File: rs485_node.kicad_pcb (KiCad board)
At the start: 2 copper layers, 53 x 18 mm, 36 parts, among them J1 Conn_01x03_Male, J2 Conn_01x04_Male, J3 Conn_01x06_Male, SW1 SW_DIP_x03, U1 SHT40, U2 ATtiny214-SS, U3 ST485EBDR, U4 MIC5504-3.3YM5

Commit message: bjt, two conns
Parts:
- removed C7: 10n, Capacitor_SMD:C_0603_1608Metric
- added J4: Conn_01x04_Male, Connector_PinHeader_2.54mm:PinHeader_1x04_P2.54mm_Vertical, F.Cu at (189.0, 58.5)
- added Q1: BC817, Package_TO_SOT_SMD:SOT-23, F.Cu at (140.0, 59.0)
- added R10: R, Resistor_SMD:R_0603_1608Metric, F.Cu at (142.8, 58.8)
- added REF**: MountingHole_4.5mm, MountingHole:MountingHole_4.5mm, F.Cu at (194.5, 68.2)
- added REF**: MountingHole_4.5mm, MountingHole:MountingHole_4.5mm, F.Cu at (194.5, 57.8)
- moved R4 4.56 mm to (145.0, 58.2), turned to 45 degrees
- moved R5 0.50 mm to (140.5, 62.0)
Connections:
- R4 pad 1: Net-(J3-Pad2) -> Net-(Q1-Pad1)
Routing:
- net GND: track 28.4 -> 36.4 mm
- net Net-(R3-Pad2): track 17.1 -> 11.9 mm
- net Net-(C3-Pad1): track 13.9 -> 18.9 mm
- net Net-(C11-Pad1): track 5.62 -> 10.6 mm
- net Net-(C10-Pad1): track 5.62 -> 10.6 mm
- net Net-(Q1-Pad1): track 0.00 -> 3.88 mm
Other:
- board size 53 x 18 mm -> 67.8 x 18 mm

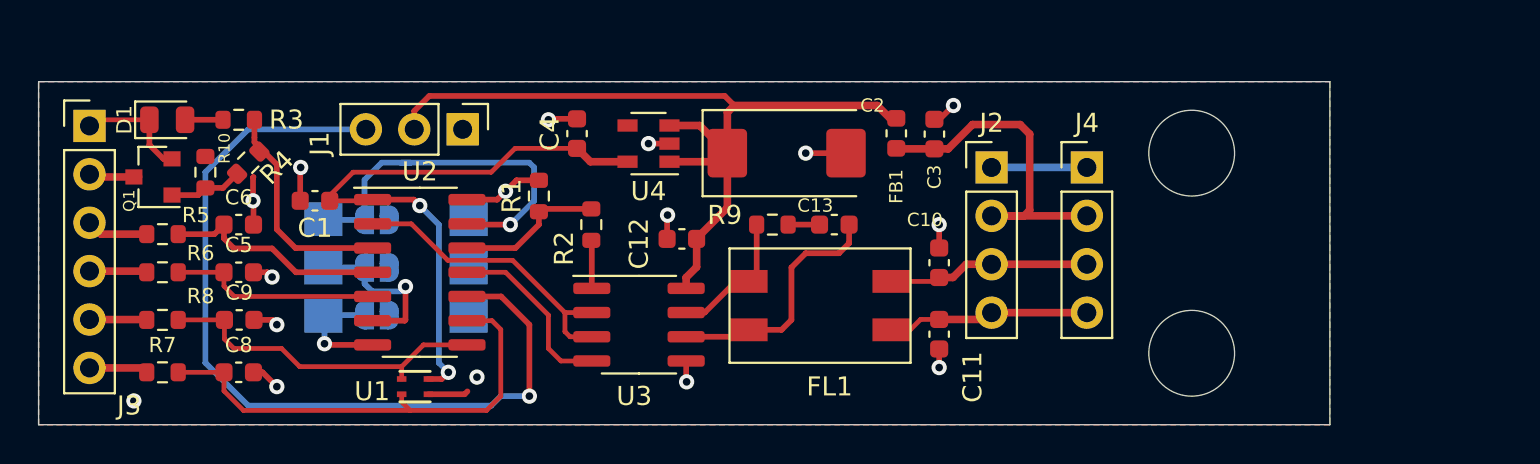
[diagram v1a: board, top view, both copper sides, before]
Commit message: new layout, removed dip-switch
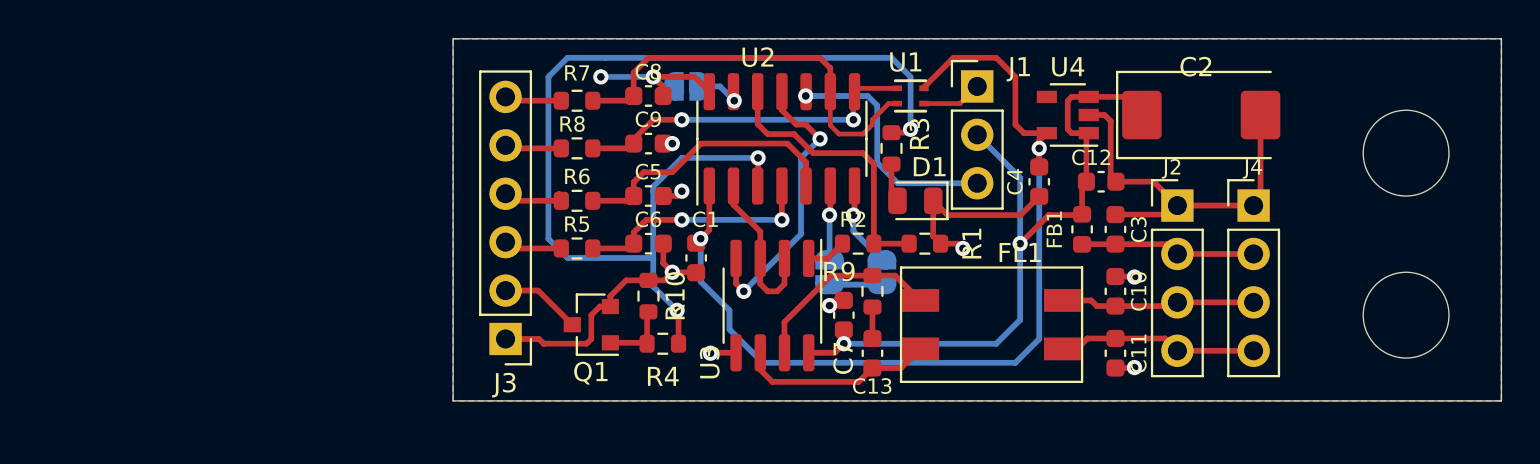
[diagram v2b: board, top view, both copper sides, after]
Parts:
- removed SW1: SW_DIP_x03, Package_DIP:SMDIP-6_W7.62mm
- added C7: 100n, Capacitor_SMD:C_0603_1608Metric, F.Cu at (176.2, 66.2)
- moved D1 39.5 mm to (180.0, 60.2), turned to 180 degrees
- moved R3 34.3 mm to (178.8, 57.5), turned to 90 degrees
- moved U1 30.1 mm to (179.8, 54.8)
- moved J1 27.1 mm to (183.2, 54.2), turned to 0 degrees
- moved JP3 26.6 mm to (178.2, 64.0), turned to 270 degrees
- moved R7 26.0 mm to (162.2, 55.0)
- moved C8 25.9 mm to (166.0, 54.8)
- moved J3 24.5 mm to (158.5, 67.5), turned to 180 degrees
- moved C4 24.4 mm to (186.5, 59.2), turned to 270 degrees
- moved Q1 24.3 mm to (163.0, 66.8)
- moved R10 24.1 mm to (166.0, 65.2)
- moved JP2 23.8 mm to (175.5, 64.0), turned to 270 degrees
- moved R4 23.7 mm to (166.8, 67.8), turned to 0 degrees
- moved R8 23.5 mm to (162.2, 57.5)
- moved C9 23.4 mm to (166.0, 57.2)
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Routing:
- net Net-(R3-Pad2): track 11.9 -> 55.0 mm, vias 0 -> 3
- net Net-(J1-Pad3): track 45.1 -> 12.9 mm
- net GND: track 36.4 -> 65.4 mm, vias 16 -> 10
- net Net-(JP1-Pad1): track 20.0 -> 2.65 mm
- net Net-(C1-Pad1): track 32.7 -> 48.4 mm
- net Net-(C3-Pad1): track 18.9 -> 9.22 mm
- net Net-(U2-Pad2): track 16.0 -> 8.65 mm
- net Net-(R1-Pad1): track 7.77 -> 14.7 mm
- net Net-(U2-Pad11): track 9.50 -> 15.9 mm, vias 0 -> 2
- net Net-(C12-Pad1): track 44.6 -> 38.5 mm, vias 0 -> 2
- net Net-(JP2-Pad1): track 9.83 -> 3.89 mm
- net Net-(C5-Pad1): track 11.2 -> 14.5 mm
- net Net-(C8-Pad1): track 25.1 -> 21.8 mm
- net Net-(FL1-Pad3): track 7.11 -> 10.3 mm
- net Net-(C13-Pad2): track 13.2 -> 10.3 mm
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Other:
- board size 67.8 x 18 mm -> 55 x 19 mm
